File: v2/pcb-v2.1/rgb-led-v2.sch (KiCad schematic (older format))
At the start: 11 parts, among them SW1 SPST

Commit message: Update pcb-v2.1 to kicad4
I just opened the project with kicad4 and it needed to change some
components and I needed to remove the "special" library. Also kicad
created a "rescue" library.
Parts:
- UC1: symbol ARDUINO_NANO -> arduino_nano
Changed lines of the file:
@@
 EESchema Schematic File Version 2
+LIBS:rgb-led-v2-rescue
 LIBS:power
 LIBS:device
@@
 LIBS:memory
 LIBS:xilinx
-LIBS:special
 LIBS:microcontrollers
 LIBS:dsp
@@
 LIBS:arduino-nano
 LIBS:rgb-led-v2-cache
-EELAYER 27 0
+EELAYER 25 0
 EELAYER END
 $Descr User 8268 5846
@@
 $EndComp
 $Comp
-L ARDUINO_NANO UC1
+L arduino_nano UC1
 U 1 1 54776301
 P 3400 2650
@@
 $EndComp
 $Comp
-L GND #PWR01
+L GND-RESCUE-rgb-led-v2 #PWR01
 U 1 1 5477A4E7
 P 4850 1800
@@
 $EndComp
 $Comp
-L GND #PWR02
+L GND-RESCUE-rgb-led-v2 #PWR02
 U 1 1 5477A4F4
 P 4850 2700
@@
 $EndComp
 $Comp
-L GND #PWR05
+L GND-RESCUE-rgb-led-v2 #PWR05
 U 1 1 5477A965
 P 1900 3300
@@
 $EndComp
 $Comp
-L GND #PWR06
+L GND-RESCUE-rgb-led-v2 #PWR06
 U 1 1 5477A96B
 P 1900 2800
@@
 $EndComp
 $Comp
-L GND #PWR07
+L GND-RESCUE-rgb-led-v2 #PWR07
 U 1 1 5477A971
 P 1900 2300
@@
 $EndComp
 $Comp
-L GND #PWR08
+L GND-RESCUE-rgb-led-v2 #PWR08
 U 1 1 5477AAB7
 P 3400 4200
@@
 $EndComp
 $Comp
-L GND #PWR010
+L GND-RESCUE-rgb-led-v2 #PWR010
 U 1 1 547A1B66
 P 1200 1150
@@
 $EndComp
 $Comp
-L GND #PWR011
+L GND-RESCUE-rgb-led-v2 #PWR011
 U 1 1 5477A4FA
 P 4850 3600

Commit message: Open project again and save it
At this point I'm a bit confused about what KiCad is doing exactly...
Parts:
- RV1, RV2, RV3: symbol POT -> POT-RESCUE-rgb-led-v2
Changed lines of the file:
@@
 $EndComp
 $Comp
-L POT RV1
+L POT-RESCUE-rgb-led-v2 RV1
 U 1 1 54775FF7
 P 1300 2200
@@
 $EndComp
 $Comp
-L POT RV2
+L POT-RESCUE-rgb-led-v2 RV2
 U 1 1 54776051
 P 1300 2700
@@
 $EndComp
 $Comp
-L POT RV3
+L POT-RESCUE-rgb-led-v2 RV3
 U 1 1 54776057
 P 1300 3200

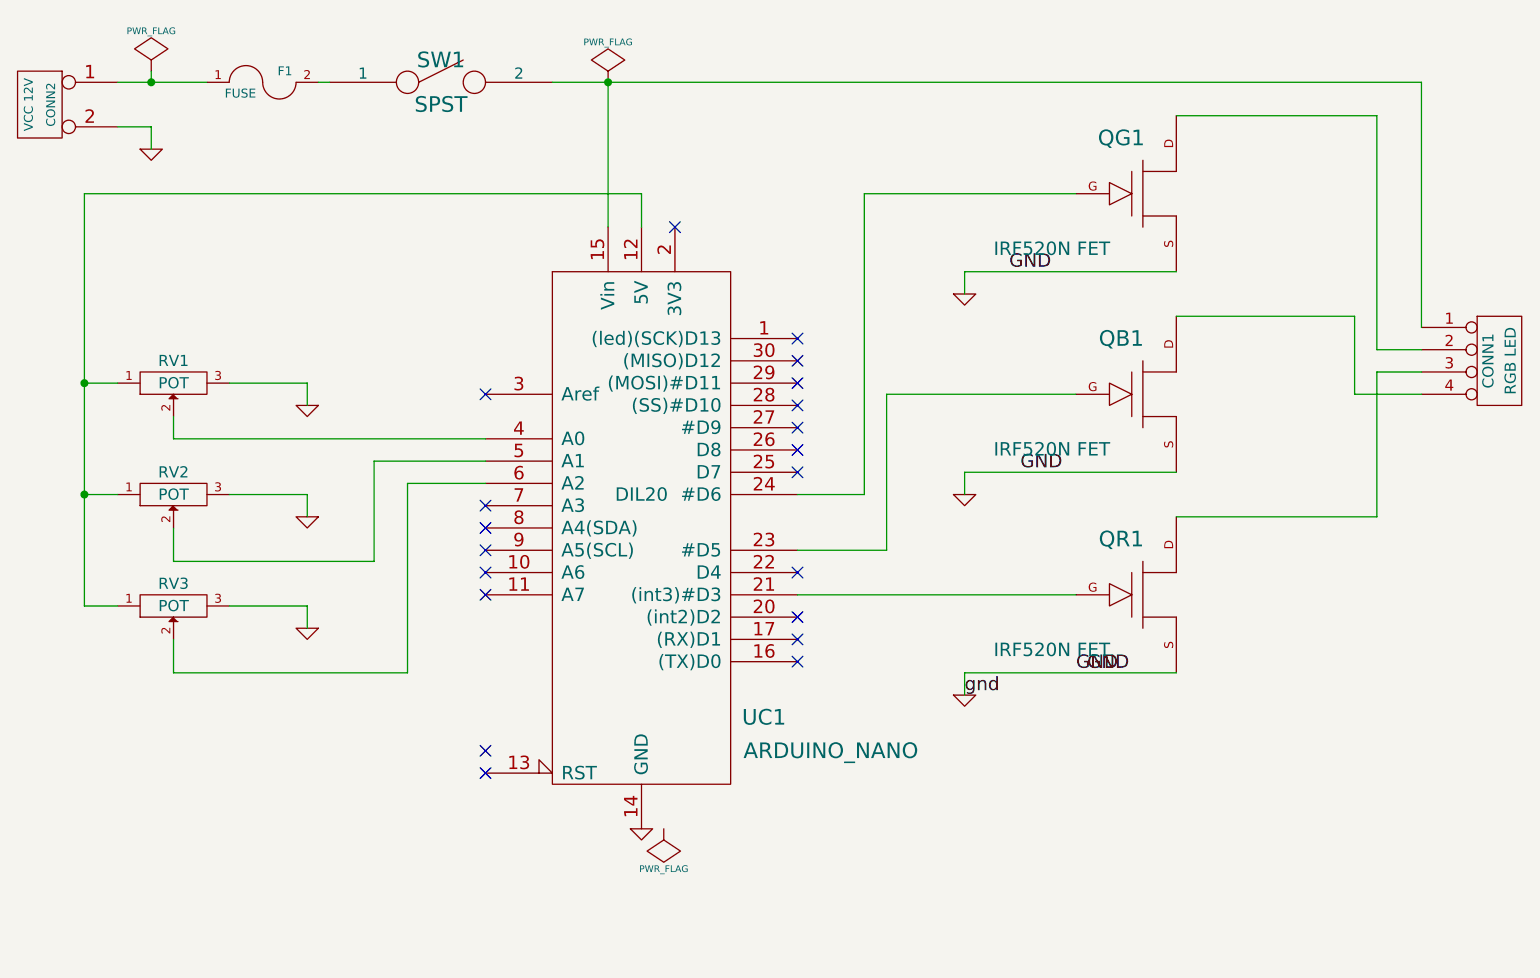
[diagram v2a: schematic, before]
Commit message: Fixed power flags to make ERC happy
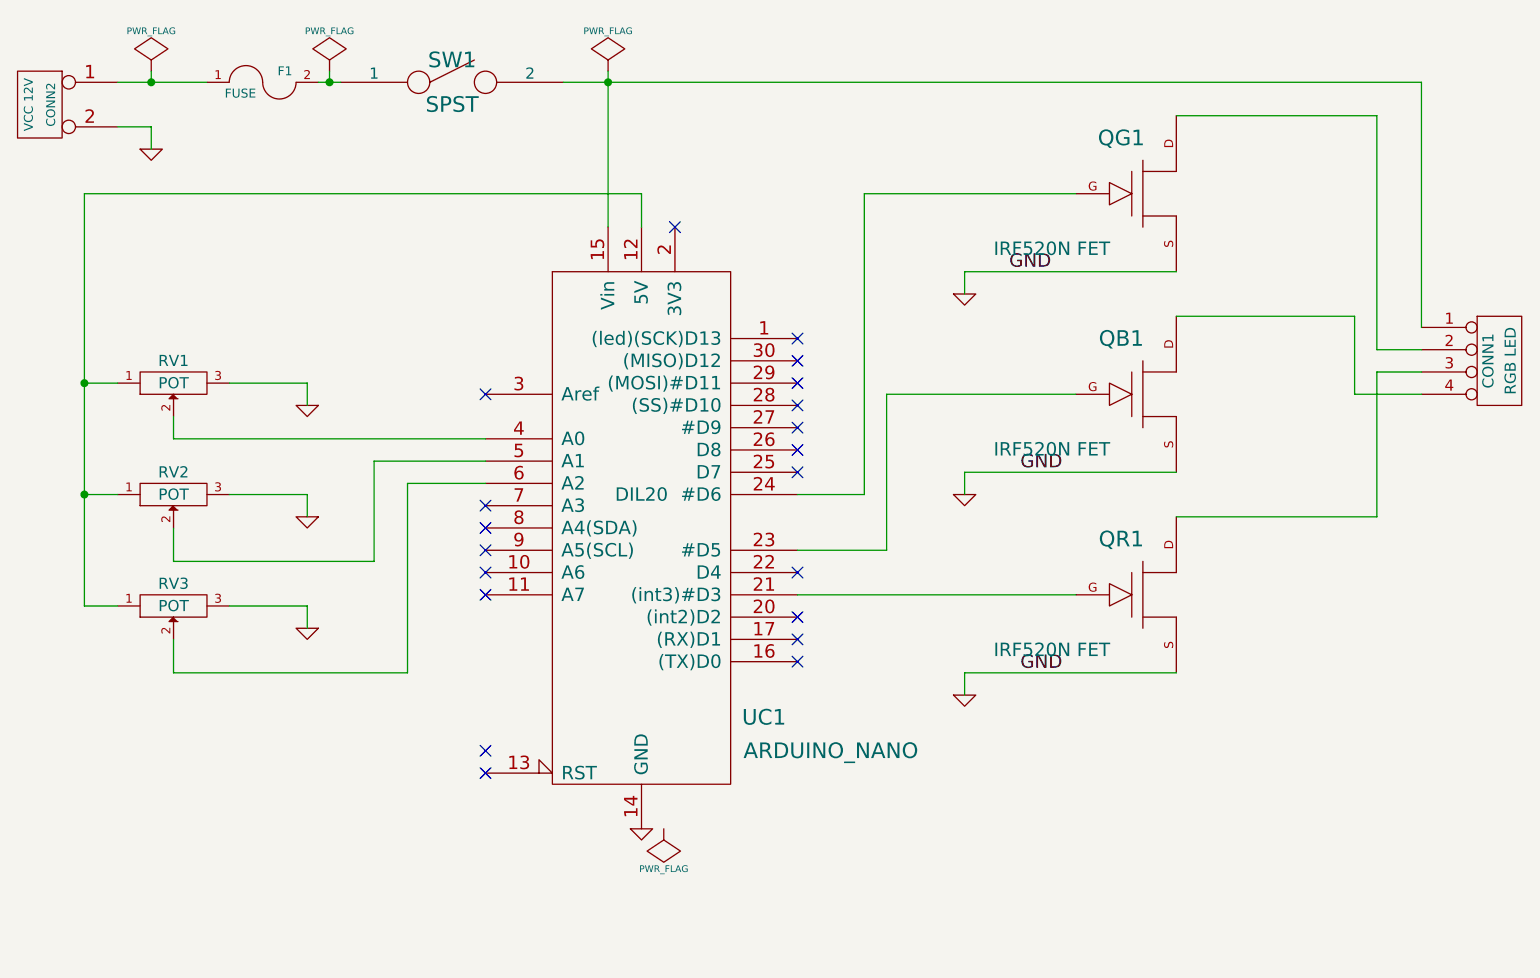
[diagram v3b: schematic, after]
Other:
- moved on the sheet: SW1
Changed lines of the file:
@@
 L PWR_FLAG #FLG09
 U 1 1 547837AB
-P 3250 850
-F 0 "#FLG09" H 3250 945 30  0001 C CNN
-F 1 "PWR_FLAG" H 3250 1030 30  0000 C CNN
-F 2 "" H 3250 850 60  0000 C CNN
-F 3 "" H 3250 850 60  0000 C CNN
-	1    3250 850
+P 3250 800
+F 0 "#FLG09" H 3250 895 30  0001 C CNN
+F 1 "PWR_FLAG" H 3250 980 30  0000 C CNN
+F 2 "" H 3250 800 60  0000 C CNN
+F 3 "" H 3250 800 60  0000 C CNN
+	1    3250 800
 	1    0    0    -1
 $EndComp
@@
 	1    0    0    -1
 $EndComp
-Text Label 5350 3500 0    60   ~ 0
-GND
-Text Label 5400 3500 0    60   ~ 0
+Text Label 5100 3500 0    60   ~ 0
 GND
 Text Label 5050 1700 0    60   ~ 0
@@
 Text Label 5100 2600 0    60   ~ 0
 GND
-Text Label 4850 3600 0    60   ~ 0
-gnd
 $Comp
 L SPST SW1
 U 1 1 547836EC
-P 2500 850
-F 0 "SW1" H 2500 950 70  0000 C CNN
-F 1 "SPST" H 2500 750 70  0000 C CNN
-F 2 "~" H 2500 850 60  0000 C CNN
-F 3 "~" H 2500 850 60  0000 C CNN
-	1    2500 850
+P 2550 850
+F 0 "SW1" H 2550 950 70  0000 C CNN
+F 1 "SPST" H 2550 750 70  0000 C CNN
+F 2 "~" H 2550 850 60  0000 C CNN
+F 3 "~" H 2550 850 60  0000 C CNN
+	1    2550 850
 	1    0    0    -1
 $EndComp
@@
 	1050 850  1450 850
 Wire Wire Line
-	3250 850  3250 1500
+	3250 800  3250 1500
 Wire Wire Line
-	3000 850  6900 850
+	3050 850  6900 850
 Wire Wire Line
 	1200 850  1200 800
@@
 	5800 3500 4850 3500
 Wire Wire Line
-	1950 850  2000 850
+	1950 850  2050 850
 $Comp
 L FUSE F1
@@
 $EndComp
 Connection ~ 3250 850
+$Comp
+L PWR_FLAG #FLG?
+U 1 1 57C56BDD
+P 2000 800
+F 0 "#FLG?" H 2000 895 30  0001 C CNN
+F 1 "PWR_FLAG" H 2000 980 30  0000 C CNN
+F 2 "" H 2000 800 60  0000 C CNN
+F 3 "" H 2000 800 60  0000 C CNN
+	1    2000 800
+	1    0    0    -1
+$EndComp
+Wire Wire Line
+	2000 800  2000 850
+Connection ~ 2000 850
 $EndSCHEMATC

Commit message: Add DC jack
Fixes #1
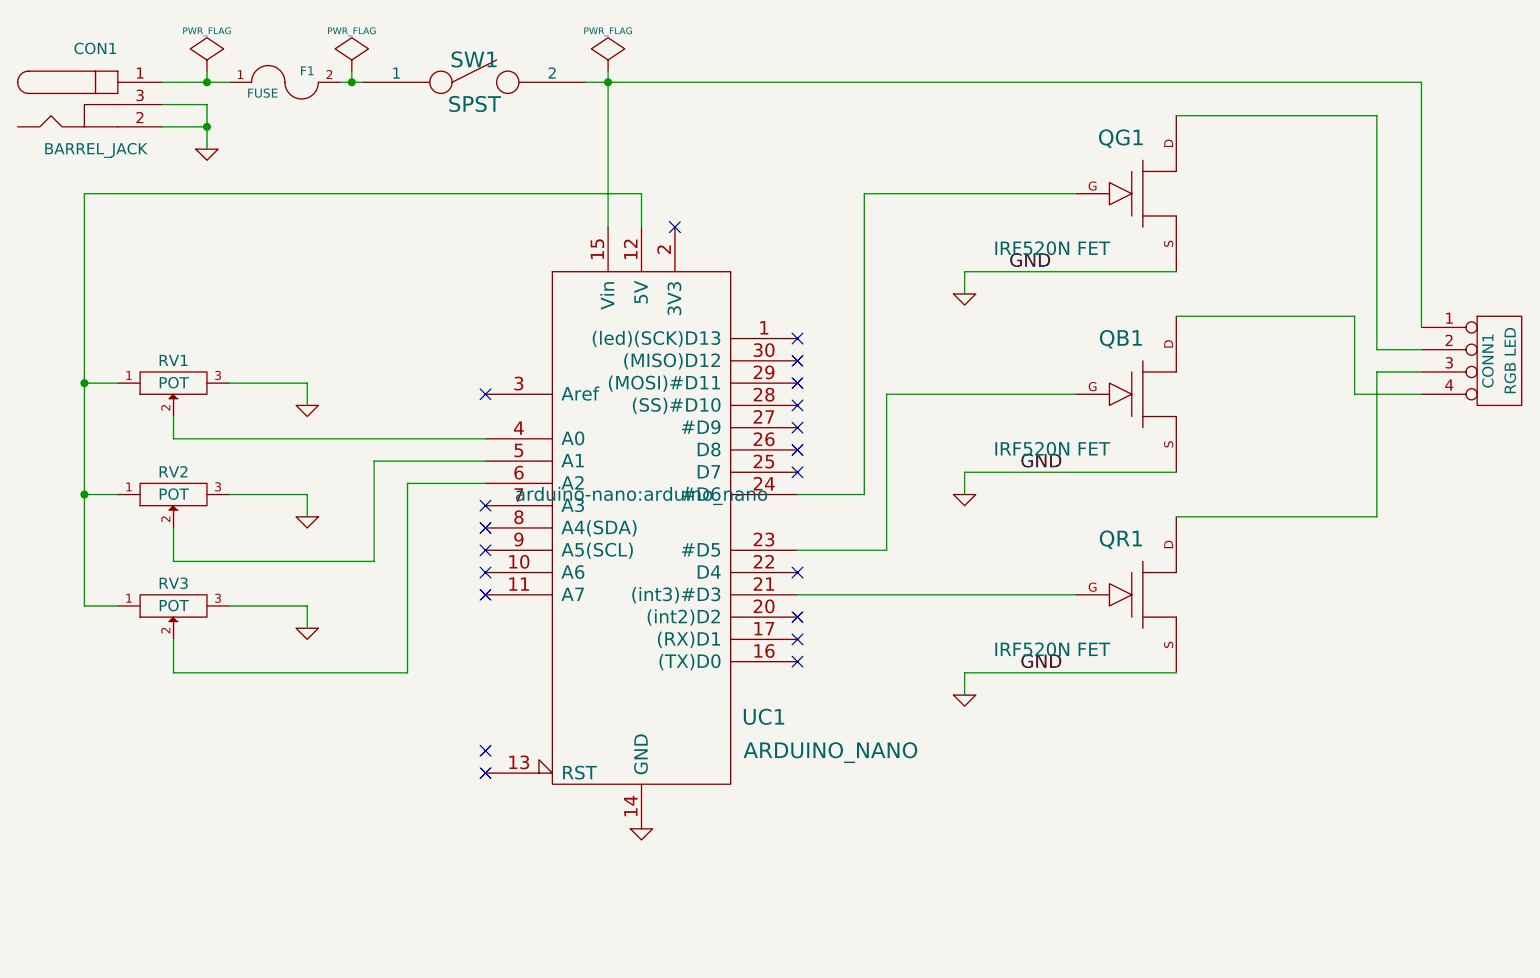
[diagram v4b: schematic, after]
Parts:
- removed CONN2: VCC 12V, ~, symbol CONN_2
- added CON1: BARREL_JACK, Connect:BARREL_JACK, symbol BARREL_JACK
- CONN1: footprint ~ -> library:PIN_ARRAY_4x1_THICK
- F1: footprint ~ -> library:KCD3
- QB1, QG1, QR1: footprint ~ -> library:IRF520N
- RV1, RV2, RV3: footprint ~ -> library:POT_3
- SW1: footprint ~ -> library:Switch_SS-12F46
- UC1: footprint DIL20 -> arduino-nano:arduino_nano
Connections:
- net GND: now also CON1.2, CON1.3
- net at F1.1: now also CON1.1
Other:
- moved on the sheet: F1, SW1
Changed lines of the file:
@@
 F 0 "QR1" H 5553 3400 70  0000 C CNN
 F 1 "IRF520N FET" H 5503 2903 60  0000 R CNN
-F 2 "~" H 5650 3150 60  0000 C CNN
+F 2 "library:IRF520N" H 5650 3150 60  0001 C CNN
 F 3 "~" H 5650 3150 60  0000 C CNN
 	1    5650 3150
@@
 F 0 "QG1" H 5553 1600 70  0000 C CNN
 F 1 "IRF520N FET" H 5503 1103 60  0000 R CNN
-F 2 "~" H 5650 1350 60  0000 C CNN
+F 2 "library:IRF520N" H 5650 1350 60  0001 C CNN
 F 3 "~" H 5650 1350 60  0000 C CNN
 	1    5650 1350
@@
 F 0 "QB1" H 5553 2500 70  0000 C CNN
 F 1 "IRF520N FET" H 5503 2003 60  0000 R CNN
-F 2 "~" H 5650 2250 60  0000 C CNN
+F 2 "library:IRF520N" H 5650 2250 60  0001 C CNN
 F 3 "~" H 5650 2250 60  0000 C CNN
 	1    5650 2250
@@
 F 0 "CONN1" V 7200 2100 50  0000 C CNN
 F 1 "RGB LED" V 7300 2100 50  0000 C CNN
-F 2 "~" H 7250 2100 60  0000 C CNN
+F 2 "library:PIN_ARRAY_4x1_THICK" H 7250 2100 60  0001 C CNN
 F 3 "~" H 7250 2100 60  0000 C CNN
 	1    7250 2100
@@
 F 0 "RV1" H 1300 2100 50  0000 C CNN
 F 1 "POT" H 1300 2200 50  0000 C CNN
-F 2 "~" H 1300 2200 60  0000 C CNN
+F 2 "library:POT_3" H 1300 2200 60  0001 C CNN
 F 3 "~" H 1300 2200 60  0000 C CNN
 	1    1300 2200
@@
 F 0 "RV2" H 1300 2600 50  0000 C CNN
 F 1 "POT" H 1300 2700 50  0000 C CNN
-F 2 "~" H 1300 2700 60  0000 C CNN
+F 2 "library:POT_3" H 1300 2700 60  0001 C CNN
 F 3 "~" H 1300 2700 60  0000 C CNN
 	1    1300 2700
@@
 F 0 "RV3" H 1300 3100 50  0000 C CNN
 F 1 "POT" H 1300 3200 50  0000 C CNN
-F 2 "~" H 1300 3200 60  0000 C CNN
+F 2 "library:POT_3" H 1300 3200 60  0001 C CNN
 F 3 "~" H 1300 3200 60  0000 C CNN
 	1    1300 3200
@@
 F 0 "UC1" H 3950 1600 70  0000 C CNN
 F 1 "ARDUINO_NANO" H 4250 1450 70  0000 C CNN
-F 2 "DIL20" H 3400 2600 60  0000 C CNN
+F 2 "arduino-nano:arduino_nano" H 3400 2600 60  0000 C CNN
 F 3 "" H 3400 2650 60  0000 C CNN
 	1    3400 2650
@@
 	1    4850 2700
 	1    0    0    -1
-$EndComp
-$Comp
-L PWR_FLAG #FLG03
-U 1 1 5477A759
-P 3500 4200
-F 0 "#FLG03" H 3500 4295 30  0001 C CNN
-F 1 "PWR_FLAG" H 3500 4380 30  0000 C CNN
-F 2 "" H 3500 4200 60  0000 C CNN
-F 3 "" H 3500 4200 60  0000 C CNN
-	1    3500 4200
-	-1   0    0    1
 $EndComp
 NoConn ~ 2700 2250
@@
 NoConn ~ 2700 3850
 $Comp
-L PWR_FLAG #FLG04
+L PWR_FLAG #FLG03
 U 1 1 5477AA91
-P 1200 800
-F 0 "#FLG04" H 1200 895 30  0001 C CNN
-F 1 "PWR_FLAG" H 1200 980 30  0000 C CNN
-F 2 "" H 1200 800 60  0000 C CNN
-F 3 "" H 1200 800 60  0000 C CNN
-	1    1200 800
-	1    0    0    -1
-$EndComp
-$Comp
-L GND-RESCUE-rgb-led-v2 #PWR05
+P 1450 800
+F 0 "#FLG03" H 1450 895 30  0001 C CNN
+F 1 "PWR_FLAG" H 1450 980 30  0000 C CNN
+F 2 "" H 1450 800 60  0000 C CNN
+F 3 "" H 1450 800 60  0000 C CNN
+	1    1450 800
+	1    0    0    -1
+$EndComp
+$Comp
+L GND-RESCUE-rgb-led-v2 #PWR04
 U 1 1 5477A965
 P 1900 3300
-F 0 "#PWR05" H 1900 3300 30  0001 C CNN
+F 0 "#PWR04" H 1900 3300 30  0001 C CNN
 F 1 "GND" H 1900 3230 30  0001 C CNN
 F 2 "" H 1900 3300 60  0000 C CNN
@@
 $EndComp
 $Comp
-L GND-RESCUE-rgb-led-v2 #PWR06
+L GND-RESCUE-rgb-led-v2 #PWR05
 U 1 1 5477A96B
 P 1900 2800
-F 0 "#PWR06" H 1900 2800 30  0001 C CNN
+F 0 "#PWR05" H 1900 2800 30  0001 C CNN
 F 1 "GND" H 1900 2730 30  0001 C CNN
 F 2 "" H 1900 2800 60  0000 C CNN
@@
 $EndComp
 $Comp
-L GND-RESCUE-rgb-led-v2 #PWR07
+L GND-RESCUE-rgb-led-v2 #PWR06
 U 1 1 5477A971
 P 1900 2300
-F 0 "#PWR07" H 1900 2300 30  0001 C CNN
+F 0 "#PWR06" H 1900 2300 30  0001 C CNN
 F 1 "GND" H 1900 2230 30  0001 C CNN
 F 2 "" H 1900 2300 60  0000 C CNN
@@
 $EndComp
 $Comp
-L GND-RESCUE-rgb-led-v2 #PWR08
+L GND-RESCUE-rgb-led-v2 #PWR07
 U 1 1 5477AAB7
 P 3400 4200
-F 0 "#PWR08" H 3400 4200 30  0001 C CNN
+F 0 "#PWR07" H 3400 4200 30  0001 C CNN
 F 1 "GND" H 3400 4130 30  0001 C CNN
 F 2 "" H 3400 4200 60  0000 C CNN
@@
 $EndComp
 $Comp
-L PWR_FLAG #FLG09
+L PWR_FLAG #FLG08
 U 1 1 547837AB
 P 3250 800
-F 0 "#FLG09" H 3250 895 30  0001 C CNN
+F 0 "#FLG08" H 3250 895 30  0001 C CNN
 F 1 "PWR_FLAG" H 3250 980 30  0000 C CNN
 F 2 "" H 3250 800 60  0000 C CNN
@@
 $EndComp
 $Comp
-L CONN_2 CONN2
-U 1 1 547A1B2B
-P 700 950
-F 0 "CONN2" V 650 950 40  0000 C CNN
-F 1 "VCC 12V" V 750 950 40  0000 C CNN
-F 2 "~" H 700 950 60  0000 C CNN
-F 3 "~" H 700 950 60  0000 C CNN
-	1    700  950
-	-1   0    0    -1
+L GND-RESCUE-rgb-led-v2 #PWR09
+U 1 1 547A1B66
+P 1450 1150
+F 0 "#PWR09" H 1450 1150 30  0001 C CNN
+F 1 "GND" H 1450 1080 30  0001 C CNN
+F 2 "" H 1450 1150 60  0000 C CNN
+F 3 "" H 1450 1150 60  0000 C CNN
+	1    1450 1150
+	1    0    0    -1
 $EndComp
 $Comp
 L GND-RESCUE-rgb-led-v2 #PWR010
-U 1 1 547A1B66
-P 1200 1150
-F 0 "#PWR010" H 1200 1150 30  0001 C CNN
-F 1 "GND" H 1200 1080 30  0001 C CNN
-F 2 "" H 1200 1150 60  0000 C CNN
-F 3 "" H 1200 1150 60  0000 C CNN
-	1    1200 1150
-	1    0    0    -1
-$EndComp
-$Comp
-L GND-RESCUE-rgb-led-v2 #PWR011
 U 1 1 5477A4FA
 P 4850 3600
-F 0 "#PWR011" H 4850 3600 30  0001 C CNN
+F 0 "#PWR010" H 4850 3600 30  0001 C CNN
 F 1 "GND" H 4850 3530 30  0001 C CNN
 F 2 "" H 4850 3600 60  0000 C CNN
@@
 L SPST SW1
 U 1 1 547836EC
-P 2550 850
-F 0 "SW1" H 2550 950 70  0000 C CNN
-F 1 "SPST" H 2550 750 70  0000 C CNN
-F 2 "~" H 2550 850 60  0000 C CNN
-F 3 "~" H 2550 850 60  0000 C CNN
-	1    2550 850
+P 2650 850
+F 0 "SW1" H 2650 950 70  0000 C CNN
+F 1 "SPST" H 2650 750 70  0000 C CNN
+F 2 "library:Switch_SS-12F46" H 2650 850 60  0001 C CNN
+F 3 "~" H 2650 850 60  0000 C CNN
+	1    2650 850
 	1    0    0    -1
 $EndComp
@@
 	4850 2600 4850 2700
 Wire Wire Line
-	1050 850  1450 850
-Wire Wire Line
-	3250 800  3250 1500
-Wire Wire Line
-	3050 850  6900 850
-Wire Wire Line
-	1200 850  1200 800
-Connection ~ 1200 850
+	1250 850  1550 850
+Wire Wire Line
+	3150 850  6900 850
+Wire Wire Line
+	1450 850  1450 800
+Connection ~ 1450 850
 Wire Wire Line
 	1900 2200 1900 2300
@@
 	1900 2200 1550 2200
 Wire Wire Line
-	1050 1050 1200 1050
-Wire Wire Line
-	1200 1050 1200 1150
+	1250 1050 1450 1050
+Wire Wire Line
+	1450 950  1450 1150
 Wire Wire Line
 	4850 3500 4850 3600
@@
 	5800 3500 4850 3500
 Wire Wire Line
-	1950 850  2050 850
+	2050 850  2150 850
 $Comp
 L FUSE F1
 U 1 1 547B0358
-P 1700 850
-F 0 "F1" H 1800 900 40  0000 C CNN
-F 1 "FUSE" H 1600 800 40  0000 C CNN
-F 2 "~" H 1700 850 60  0000 C CNN
-F 3 "~" H 1700 850 60  0000 C CNN
-	1    1700 850
+P 1800 850
+F 0 "F1" H 1900 900 40  0000 C CNN
+F 1 "FUSE" H 1700 800 40  0000 C CNN
+F 2 "library:KCD3" H 1800 850 60  0001 C CNN
+F 3 "~" H 1800 850 60  0000 C CNN
+	1    1800 850
 	1    0    0    -1
 $EndComp
 Connection ~ 3250 850
 $Comp
-L PWR_FLAG #FLG?
+L PWR_FLAG #FLG011
 U 1 1 57C56BDD
-P 2000 800
-F 0 "#FLG?" H 2000 895 30  0001 C CNN
-F 1 "PWR_FLAG" H 2000 980 30  0000 C CNN
-F 2 "" H 2000 800 60  0000 C CNN
-F 3 "" H 2000 800 60  0000 C CNN
-	1    2000 800
-	1    0    0    -1
-$EndComp
-Wire Wire Line
-	2000 800  2000 850
-Connection ~ 2000 850
+P 2100 800
+F 0 "#FLG011" H 2100 895 30  0001 C CNN
+F 1 "PWR_FLAG" H 2100 980 30  0000 C CNN
+F 2 "" H 2100 800 60  0000 C CNN
+F 3 "" H 2100 800 60  0000 C CNN
+	1    2100 800
+	1    0    0    -1
+$EndComp
+Wire Wire Line
+	2100 800  2100 850
+Connection ~ 2100 850
+$Comp
+L BARREL_JACK CON1
+U 1 1 57CC444D
+P 950 950
+F 0 "CON1" H 950 1200 50  0000 C CNN
+F 1 "BARREL_JACK" H 950 750 50  0000 C CNN
+F 2 "Connect:BARREL_JACK" H 950 950 50  0001 C CNN
+F 3 "" H 950 950 50  0000 C CNN
+	1    950  950
+	1    0    0    -1
+$EndComp
+Wire Wire Line
+	1250 950  1450 950
+Connection ~ 1450 1050
+Wire Wire Line
+	3250 800  3250 1500
 $EndSCHEMATC
